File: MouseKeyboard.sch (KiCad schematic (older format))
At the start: 17 parts

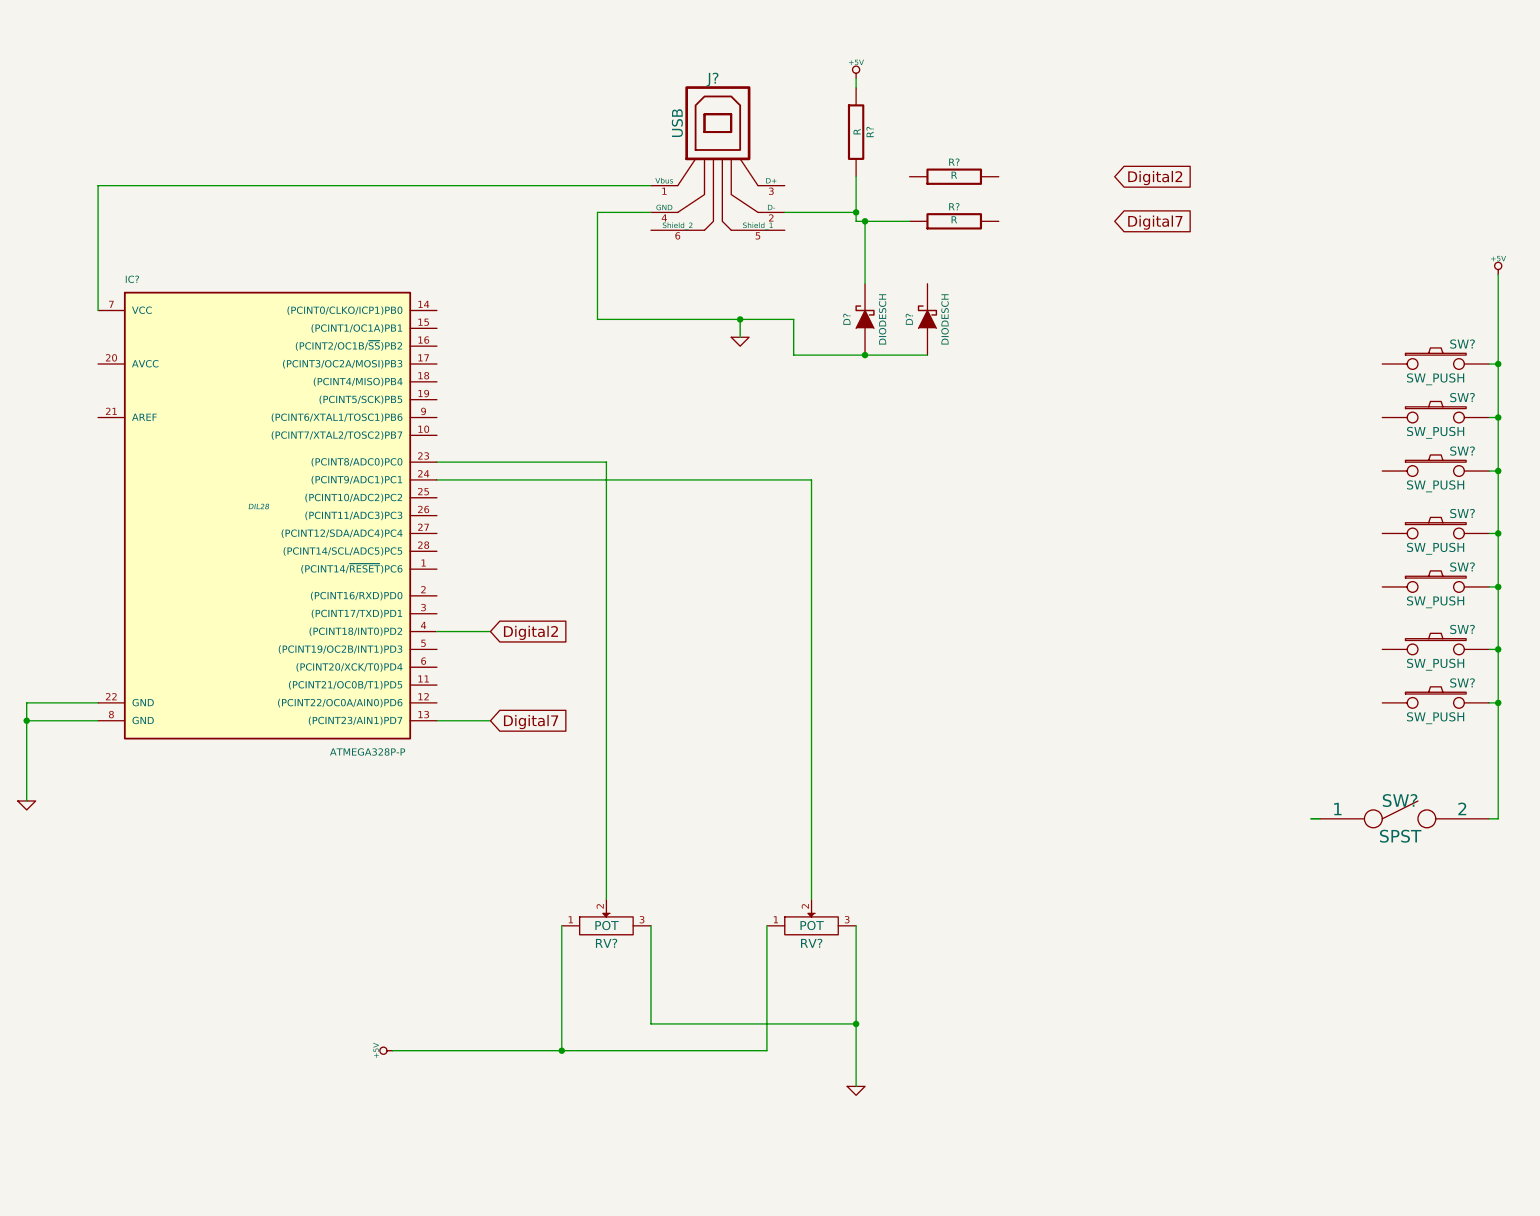
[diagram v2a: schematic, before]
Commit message: Moved Diagram Around a bit
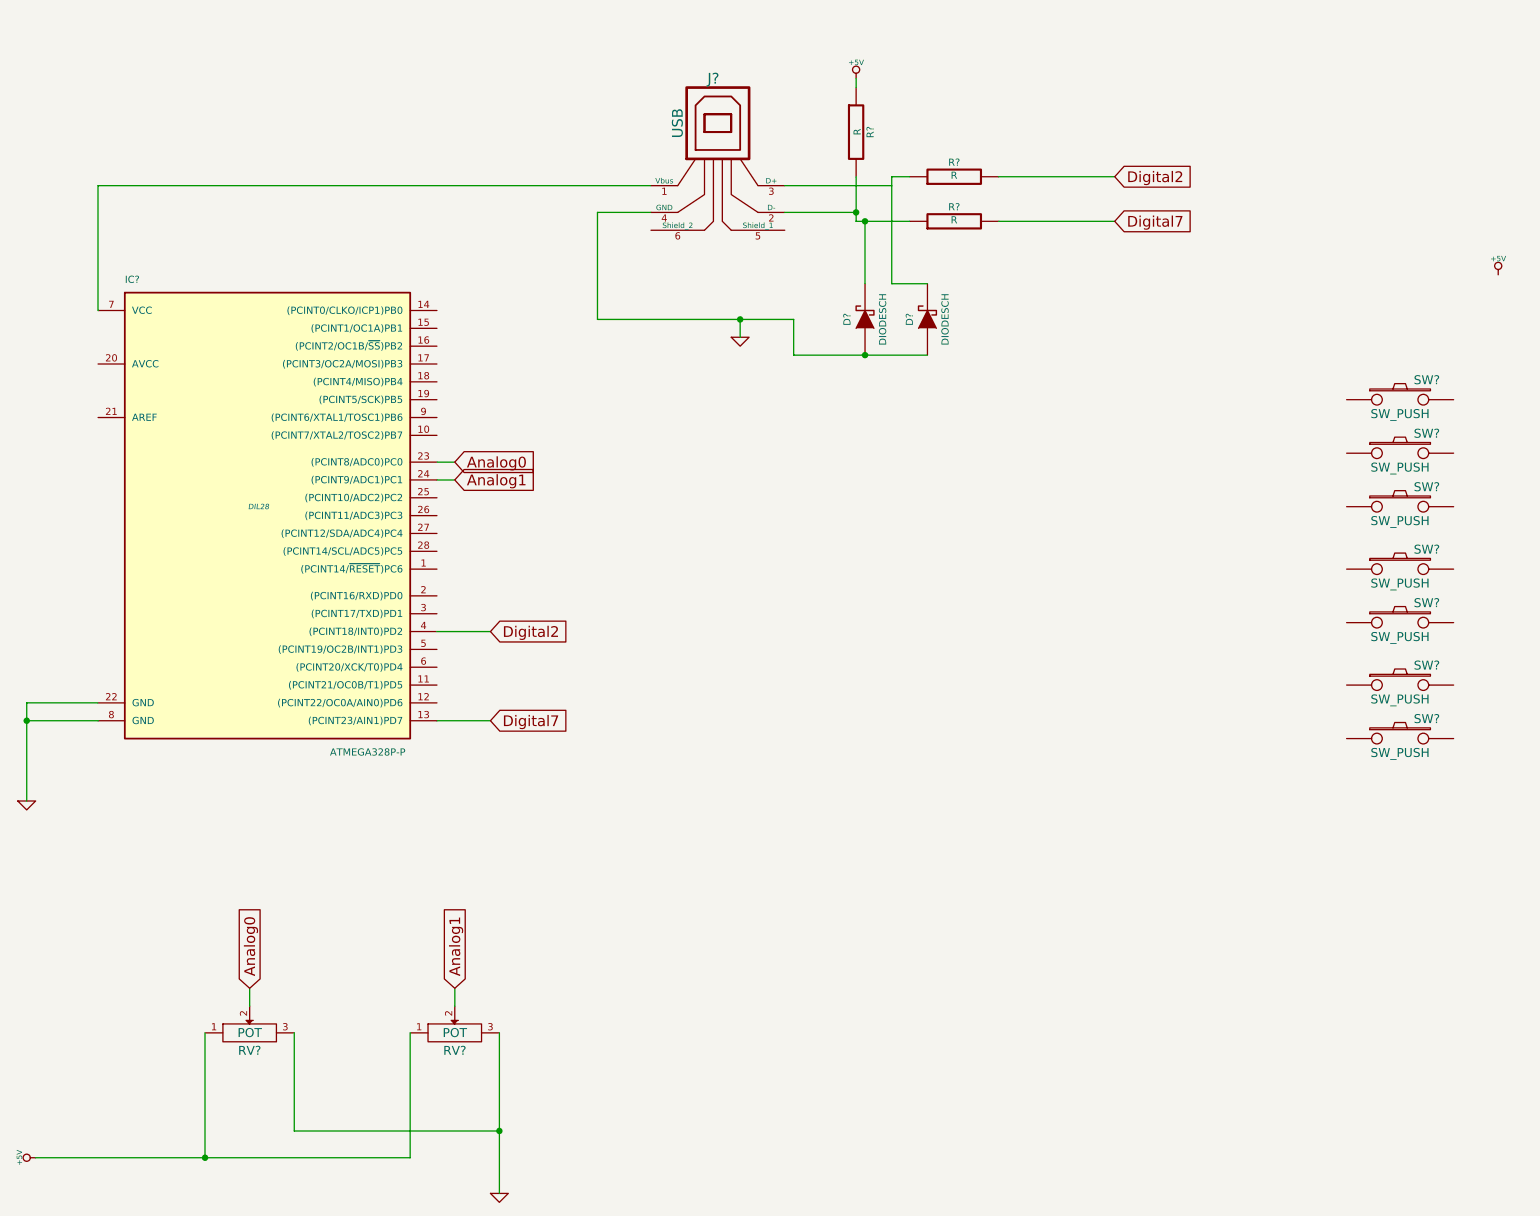
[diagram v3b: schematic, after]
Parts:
- removed SW?: SPST, symbol SPST
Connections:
- net +5V: no longer SW?.2, SW?.2, SW?.2, SW?.2, SW?.2, SW?.2, SW?.2
- net Digital2: now also R?.2
- net Digital7: now also R?.2
- net Analog0: now reaches IC?.23 ((PCINT8/ADC0)PC0), RV?.2
- net Analog1: now reaches IC?.24 ((PCINT9/ADC1)PC1), RV?.2
- net at R?.1: now also D?.2 (K)
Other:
- moved on the sheet: RV?, SW?
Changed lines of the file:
@@
 L SW_PUSH SW?
 U 1 1 54DAA625
-P 9100 2700
-F 0 "SW?" H 9250 2810 50  0000 C CNN
-F 1 "SW_PUSH" H 9100 2620 50  0000 C CNN
-F 2 "" H 9100 2700 60  0000 C CNN
-F 3 "" H 9100 2700 60  0000 C CNN
-	1    9100 2700
+P 8900 2900
+F 0 "SW?" H 9050 3010 50  0000 C CNN
+F 1 "SW_PUSH" H 8900 2820 50  0000 C CNN
+F 2 "" H 8900 2900 60  0000 C CNN
+F 3 "" H 8900 2900 60  0000 C CNN
+	1    8900 2900
 	1    0    0    -1
 $EndComp
@@
 L SW_PUSH SW?
 U 1 1 54DAA639
-P 9100 3300
-F 0 "SW?" H 9250 3410 50  0000 C CNN
-F 1 "SW_PUSH" H 9100 3220 50  0000 C CNN
-F 2 "" H 9100 3300 60  0000 C CNN
-F 3 "" H 9100 3300 60  0000 C CNN
-	1    9100 3300
+P 8900 3500
+F 0 "SW?" H 9050 3610 50  0000 C CNN
+F 1 "SW_PUSH" H 8900 3420 50  0000 C CNN
+F 2 "" H 8900 3500 60  0000 C CNN
+F 3 "" H 8900 3500 60  0000 C CNN
+	1    8900 3500
 	1    0    0    -1
 $EndComp
@@
 L SW_PUSH SW?
 U 1 1 54DAA64D
-P 9100 3650
-F 0 "SW?" H 9250 3760 50  0000 C CNN
-F 1 "SW_PUSH" H 9100 3570 50  0000 C CNN
-F 2 "" H 9100 3650 60  0000 C CNN
-F 3 "" H 9100 3650 60  0000 C CNN
-	1    9100 3650
+P 8900 3850
+F 0 "SW?" H 9050 3960 50  0000 C CNN
+F 1 "SW_PUSH" H 8900 3770 50  0000 C CNN
+F 2 "" H 8900 3850 60  0000 C CNN
+F 3 "" H 8900 3850 60  0000 C CNN
+	1    8900 3850
 	1    0    0    -1
 $EndComp
@@
 L SW_PUSH SW?
 U 1 1 54DAA661
-P 9100 3950
-F 0 "SW?" H 9250 4060 50  0000 C CNN
-F 1 "SW_PUSH" H 9100 3870 50  0000 C CNN
-F 2 "" H 9100 3950 60  0000 C CNN
-F 3 "" H 9100 3950 60  0000 C CNN
-	1    9100 3950
+P 8900 4150
+F 0 "SW?" H 9050 4260 50  0000 C CNN
+F 1 "SW_PUSH" H 8900 4070 50  0000 C CNN
+F 2 "" H 8900 4150 60  0000 C CNN
+F 3 "" H 8900 4150 60  0000 C CNN
+	1    8900 4150
 	1    0    0    -1
 $EndComp
@@
 L SW_PUSH SW?
 U 1 1 54DAA675
-P 9100 4300
-F 0 "SW?" H 9250 4410 50  0000 C CNN
-F 1 "SW_PUSH" H 9100 4220 50  0000 C CNN
-F 2 "" H 9100 4300 60  0000 C CNN
-F 3 "" H 9100 4300 60  0000 C CNN
-	1    9100 4300
-	1    0    0    -1
-$EndComp
-$Comp
-L SPST SW?
-U 1 1 54DAA689
-P 8900 5250
-F 0 "SW?" H 8900 5350 70  0000 C CNN
-F 1 "SPST" H 8900 5150 70  0000 C CNN
-F 2 "" H 8900 5250 60  0000 C CNN
-F 3 "" H 8900 5250 60  0000 C CNN
-	1    8900 5250
+P 8900 4500
+F 0 "SW?" H 9050 4610 50  0000 C CNN
+F 1 "SW_PUSH" H 8900 4420 50  0000 C CNN
+F 2 "" H 8900 4500 60  0000 C CNN
+F 3 "" H 8900 4500 60  0000 C CNN
+	1    8900 4500
 	1    0    0    -1
 $EndComp
@@
 L SW_PUSH SW?
 U 1 1 54DAA69D
-P 9100 4600
-F 0 "SW?" H 9250 4710 50  0000 C CNN
-F 1 "SW_PUSH" H 9100 4520 50  0000 C CNN
-F 2 "" H 9100 4600 60  0000 C CNN
-F 3 "" H 9100 4600 60  0000 C CNN
-	1    9100 4600
+P 8900 4800
+F 0 "SW?" H 9050 4910 50  0000 C CNN
+F 1 "SW_PUSH" H 8900 4720 50  0000 C CNN
+F 2 "" H 8900 4800 60  0000 C CNN
+F 3 "" H 8900 4800 60  0000 C CNN
+	1    8900 4800
 	1    0    0    -1
 $EndComp
@@
 L SW_PUSH SW?
 U 1 1 54DAA6B1
-P 9100 3000
-F 0 "SW?" H 9250 3110 50  0000 C CNN
-F 1 "SW_PUSH" H 9100 2920 50  0000 C CNN
-F 2 "" H 9100 3000 60  0000 C CNN
-F 3 "" H 9100 3000 60  0000 C CNN
-	1    9100 3000
+P 8900 3200
+F 0 "SW?" H 9050 3310 50  0000 C CNN
+F 1 "SW_PUSH" H 8900 3120 50  0000 C CNN
+F 2 "" H 8900 3200 60  0000 C CNN
+F 3 "" H 8900 3200 60  0000 C CNN
+	1    8900 3200
 	1    0    0    -1
 $EndComp
@@
 L POT RV?
 U 1 1 54DAA84B
-P 4450 5850
-F 0 "RV?" H 4450 5750 50  0000 C CNN
-F 1 "POT" H 4450 5850 50  0000 C CNN
-F 2 "" H 4450 5850 60  0000 C CNN
-F 3 "" H 4450 5850 60  0000 C CNN
-	1    4450 5850
+P 2450 6450
+F 0 "RV?" H 2450 6350 50  0000 C CNN
+F 1 "POT" H 2450 6450 50  0000 C CNN
+F 2 "" H 2450 6450 60  0000 C CNN
+F 3 "" H 2450 6450 60  0000 C CNN
+	1    2450 6450
 	1    0    0    -1
 $EndComp
@@
 L POT RV?
 U 1 1 54DAA85F
-P 5600 5850
-F 0 "RV?" H 5600 5750 50  0000 C CNN
-F 1 "POT" H 5600 5850 50  0000 C CNN
-F 2 "" H 5600 5850 60  0000 C CNN
-F 3 "" H 5600 5850 60  0000 C CNN
-	1    5600 5850
+P 3600 6450
+F 0 "RV?" H 3600 6350 50  0000 C CNN
+F 1 "POT" H 3600 6450 50  0000 C CNN
+F 2 "" H 3600 6450 60  0000 C CNN
+F 3 "" H 3600 6450 60  0000 C CNN
+	1    3600 6450
 	1    0    0    -1
 $EndComp
@@
 L +5V #PWR02
 U 1 1 54DAA9EC
-P 3250 6550
-F 0 "#PWR02" H 3250 6640 20  0001 C CNN
-F 1 "+5V" H 3250 6640 30  0000 C CNN
-F 2 "" H 3250 6550 60  0000 C CNN
-F 3 "" H 3250 6550 60  0000 C CNN
-	1    3250 6550
+P 1250 7150
+F 0 "#PWR02" H 1250 7240 20  0001 C CNN
+F 1 "+5V" H 1250 7240 30  0000 C CNN
+F 2 "" H 1250 7150 60  0000 C CNN
+F 3 "" H 1250 7150 60  0000 C CNN
+	1    1250 7150
 	0    -1   -1   0
 $EndComp
@@
 L GND #PWR03
 U 1 1 54DAAA0D
-P 5850 6750
-F 0 "#PWR03" H 5850 6750 30  0001 C CNN
-F 1 "GND" H 5850 6680 30  0001 C CNN
-F 2 "" H 5850 6750 60  0000 C CNN
-F 3 "" H 5850 6750 60  0000 C CNN
-	1    5850 6750
+P 3850 7350
+F 0 "#PWR03" H 3850 7350 30  0001 C CNN
+F 1 "GND" H 3850 7280 30  0001 C CNN
+F 2 "" H 3850 7350 60  0000 C CNN
+F 3 "" H 3850 7350 60  0000 C CNN
+	1    3850 7350
 	1    0    0    -1
 $EndComp
@@
 $EndComp
 Wire Wire Line
-	3250 6550 5350 6550
-Wire Wire Line
-	4200 6550 4200 5850
-Wire Wire Line
-	5350 6550 5350 5850
-Connection ~ 4200 6550
-Wire Wire Line
-	5850 5850 5850 6750
-Wire Wire Line
-	4700 5850 4700 6400
-Wire Wire Line
-	4700 6400 5850 6400
-Connection ~ 5850 6400
-Wire Wire Line
-	9400 2700 9450 2700
-Wire Wire Line
-	9450 2200 9450 5250
-Wire Wire Line
-	9450 3000 9400 3000
-Connection ~ 9450 2700
-Wire Wire Line
-	9450 3300 9400 3300
-Connection ~ 9450 3000
-Wire Wire Line
-	9450 3650 9400 3650
-Connection ~ 9450 3300
-Wire Wire Line
-	9450 3950 9400 3950
-Connection ~ 9450 3650
-Connection ~ 9450 3950
-Wire Wire Line
-	9450 4300 9400 4300
-Wire Wire Line
-	9450 4600 9400 4600
-Connection ~ 9450 4300
-Wire Wire Line
-	9450 5250 9400 5250
-Connection ~ 9450 4600
-Wire Wire Line
-	8400 5250 8450 5250
-Wire Wire Line
-	4450 5700 4450 3250
-Wire Wire Line
-	4450 3250 3500 3250
-Wire Wire Line
-	5600 5700 5600 3350
-Wire Wire Line
-	5600 3350 3500 3350
+	1250 7150 3350 7150
+Wire Wire Line
+	2200 7150 2200 6450
+Wire Wire Line
+	3350 7150 3350 6450
+Connection ~ 2200 7150
+Wire Wire Line
+	3850 6450 3850 7350
+Wire Wire Line
+	2700 6450 2700 7000
+Wire Wire Line
+	2700 7000 3850 7000
+Connection ~ 3850 7000
 Wire Wire Line
 	1200 4600 1200 5150
@@
 Connection ~ 5200 2450
 Connection ~ 5900 2650
+Wire Wire Line
+	6050 2250 6250 2250
+Wire Wire Line
+	6050 1650 6050 2250
+Wire Wire Line
+	6050 1650 6150 1650
+Wire Wire Line
+	5450 1700 6050 1700
+Wire Wire Line
+	6650 1650 7300 1650
+Wire Wire Line
+	6650 1900 7300 1900
+Text GLabel 3600 3350 2    60   Input ~ 0
+Analog1
+Wire Wire Line
+	3600 3350 3500 3350
+Text GLabel 3600 3250 2    60   Input ~ 0
+Analog0
+Wire Wire Line
+	3500 3250 3600 3250
+Text GLabel 2450 6200 1    60   Input ~ 0
+Analog0
+Text GLabel 3600 6200 1    60   Input ~ 0
+Analog1
+Wire Wire Line
+	2450 6200 2450 6300
+Wire Wire Line
+	3600 6300 3600 6200
 $EndSCHEMATC

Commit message: Schematic is almost done
YAY!

Just have to make a bill of materials
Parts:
- gave numbers to parts that had none: 16
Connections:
- net +5V: now also SW1.2, SW2.2, SW3.2, SW4.2, SW5.2, SW6.2, SW7.2
- net at SW1.1: now also IC1.5 ((PCINT19/OC2B/INT1)PD3)
- net at SW3.1: now also IC1.11 ((PCINT21/OC0B/T1)PD5)
- net at SW4.1: now also IC1.12 ((PCINT22/OC0A/AIN0)PD6)
- net at SW5.1: now also IC1.14 ((PCINT0/CLKO/ICP1)PB0)
- net at SW6.1: now also IC1.15 ((PCINT1/OC1A)PB1)
- net at SW7.1: now also IC1.16 ((PCINT2/OC1B/~SS~)PB2)
- net at SW2.1: now also IC1.6 ((PCINT20/XCK/T0)PD4)
- net at IC1.7 (VCC): no longer J1.1 (Vbus)
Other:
- moved on the sheet: IC1, SW1, SW2, SW3, SW4, SW5, SW6, SW7
